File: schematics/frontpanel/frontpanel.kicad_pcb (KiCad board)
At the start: 2 copper layers, 72.4 x 21.6 mm, 10 parts, among them J1 Conn_01x02_Male, J2 Conn_01x02_Male, J3 Conn_01x03_Male, J4 Conn_01x03_Male, SW1 SW_Push, SW2 SW_Push

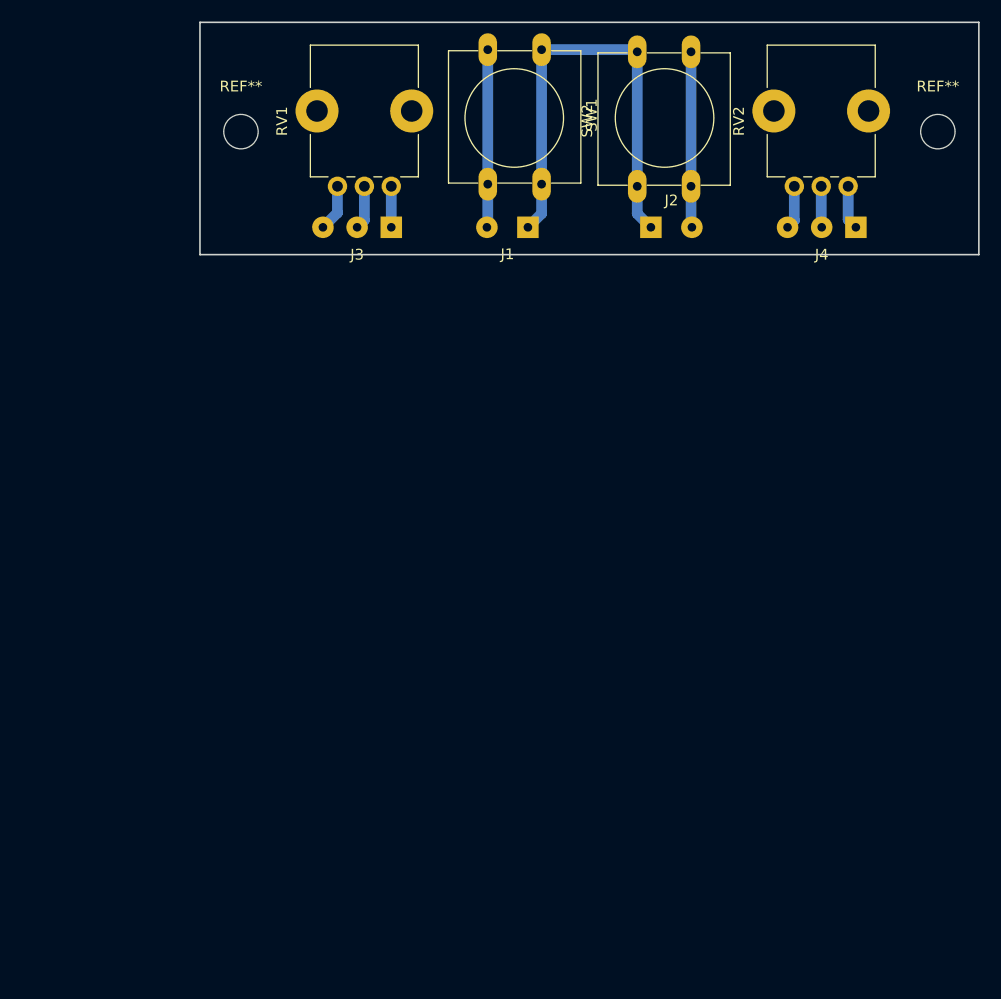
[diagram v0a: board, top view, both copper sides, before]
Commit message: Updated front panel PCB for v1
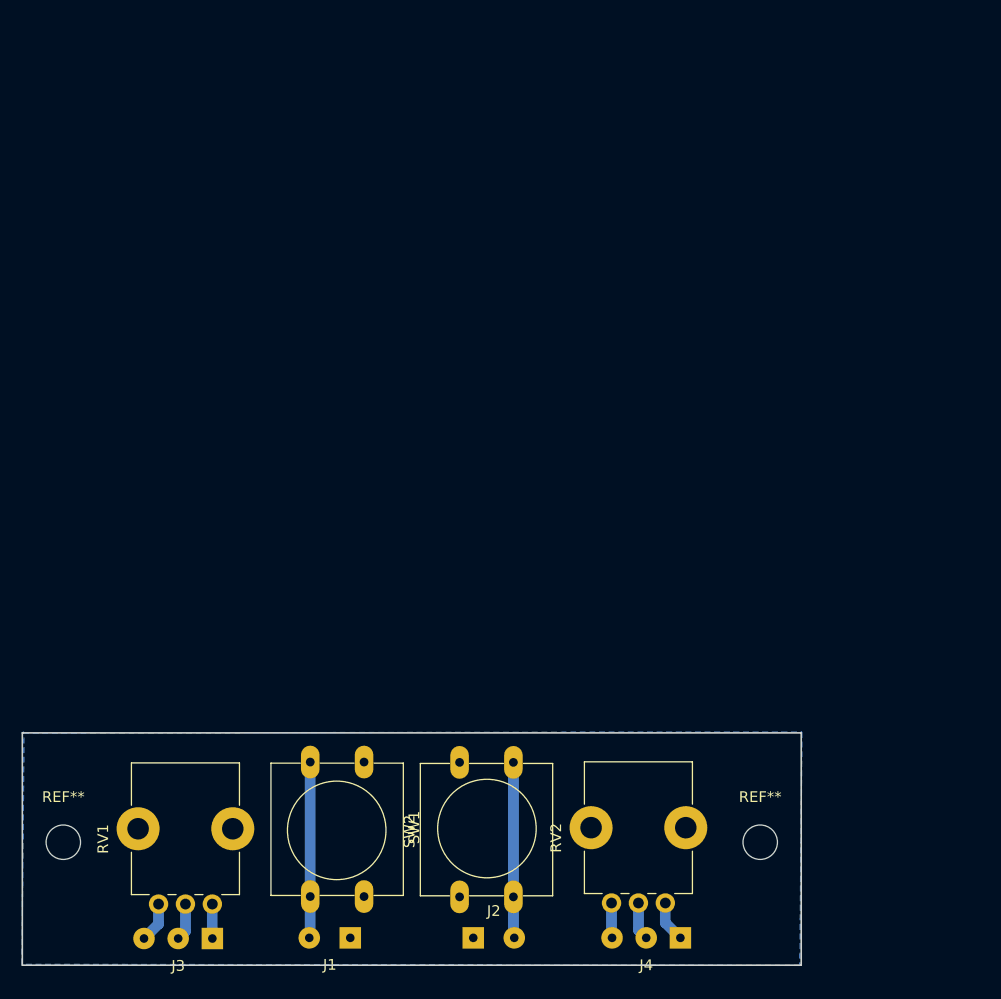
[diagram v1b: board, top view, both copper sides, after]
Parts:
- moved RV1 68.8 mm to (58.3, 126.4)
- moved RV2 68.7 mm to (100.4, 126.3)
- moved SW1 68.2 mm to (72.4, 113.2)
- moved J3 68.2 mm to (58.3, 129.6)
- moved REF** 68.1 mm to (109.2, 120.7)
- moved REF** 68.1 mm to (44.5, 120.7)
- moved SW2 68.1 mm to (81.3, 125.7)
- moved J1 68.1 mm to (71.1, 129.5)
- moved J2 68.1 mm to (82.5, 129.5)
- moved J4 68.0 mm to (101.8, 129.5)
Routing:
- net Net-(J1-Pad1): track 42.8 -> 0.28 mm
- net Net-(J4-Pad3): track 4.07 -> 3.26 mm
- net Net-(J3-Pad3): track 4.37 -> 3.76 mm
- net Net-(J3-Pad2): track 4.09 -> 3.48 mm
- net Net-(J3-Pad1): track 3.81 -> 3.20 mm
- added copper zone on B.Cu, net Net-(J1-Pad1)
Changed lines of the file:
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@@
     (thickness 1.6)
     (drawings 6)
-    (tracks 24)
+    (tracks 18)
     (zones 0)
     (modules 10)
@@
   )
   (module Potentiometer_THT:Potentiometer_Alps_RK09K_Single_Vertical (layer F.Cu)
-    (at 117.39 59.69 90)
+    (at 100.4 126.3 90)
     (descr "Potentiometer, vertical, Alps RK09K Single, http://www.alps.com/prod/info/E/HTML/Potentiometer/RotaryPotentiometers/RK09K/RK09K_list.html")
     (tags "Potentiometer vertical Alps RK09K Single")
@@
   )
   (module Connector_Wire:SolderWirePad_1x02_P3.81mm_Drill0.8mm (layer F.Cu)
-    (at 87.63 63.5 180)
+    (at 71.12 129.54 180)
     (descr "Wire solder connection")
     (tags connector)
@@
   )
   (module Connector_Wire:SolderWirePad_1x02_P3.81mm_Drill0.8mm (layer F.Cu)
-    (at 99.06 63.5)
+    (at 82.55 129.54)
     (descr "Wire solder connection")
     (tags connector)
@@
   )
   (module Connector_Wire:SolderWirePad_1x03_P3.175mm_Drill0.8mm (layer F.Cu)
-    (at 74.93 63.5 180)
+    (at 58.3 129.6 180)
     (descr "Wire solder connection")
     (tags connector)
@@
   )
   (module Connector_Wire:SolderWirePad_1x03_P3.175mm_Drill0.8mm (layer F.Cu)
-    (at 118.11 63.5 180)
+    (at 101.8 129.54 180)
     (descr "Wire solder connection")
     (tags connector)
@@
   )
   (module Potentiometer_THT:Potentiometer_Alps_RK09K_Single_Vertical (layer F.Cu)
-    (at 74.93 59.69 90)
+    (at 58.3 126.4 90)
     (descr "Potentiometer, vertical, Alps RK09K Single, http://www.alps.com/prod/info/E/HTML/Potentiometer/RotaryPotentiometers/RK09K/RK09K_list.html")
     (tags "Potentiometer vertical Alps RK09K Single")
@@
   )
   (module Button_Switch_THT:SW_PUSH-12mm (layer F.Cu)
-    (at 88.9 46.99 270)
+    (at 72.4 113.2 270)
     (descr "SW PUSH 12mm https://www.e-switch.com/system/asset/product_line/data_sheet/143/TL1100.pdf")
     (tags "tact sw push 12mm")
@@
   )
   (module Button_Switch_THT:SW_PUSH-12mm (layer F.Cu)
-    (at 97.79 59.69 90)
+    (at 81.28 125.73 90)
     (descr "SW PUSH 12mm https://www.e-switch.com/system/asset/product_line/data_sheet/143/TL1100.pdf")
     (tags "tact sw push 12mm")
@@
   )
   (module MountingHole:MountingHole_3.2mm_M3 (layer F.Cu)
-    (at 125.73 54.61)
+    (at 109.22 120.65)
     (descr "Mounting Hole 3.2mm, no annular, M3")
     (tags "mounting hole 3.2mm no annular m3")
@@
   )
   (module MountingHole:MountingHole_3.2mm_M3 (layer F.Cu)
-    (at 60.96 54.61)
+    (at 44.45 120.65)
     (descr "Mounting Hole 3.2mm, no annular, M3")
     (tags "mounting hole 3.2mm no annular m3")
@@
   )
   (dimension 21.59 (width 0.3) (layer Dwgs.User)
-    (gr_text "21,590 mm" (at 49.97 55.245 90) (layer Dwgs.User)
+    (gr_text "21,590 mm" (at 33.46 121.285 90) (layer Dwgs.User)
       (effects (font (size 1.5 1.5) (thickness 0.3)))
     )
-    (feature1 (pts (xy 57.15 44.45) (xy 51.483579 44.45)))
-    (feature2 (pts (xy 57.15 66.04) (xy 51.483579 66.04)))
-    (crossbar (pts (xy 52.07 66.04) (xy 52.07 44.45)))
-    (arrow1a (pts (xy 52.07 44.45) (xy 52.656421 45.576504)))
-    (arrow1b (pts (xy 52.07 44.45) (xy 51.483579 45.576504)))
-    (arrow2a (pts (xy 52.07 66.04) (xy 52.656421 64.913496)))
-    (arrow2b (pts (xy 52.07 66.04) (xy 51.483579 64.913496)))
+    (feature1 (pts (xy 40.64 110.49) (xy 34.973579 110.49)))
+    (feature2 (pts (xy 40.64 132.08) (xy 34.973579 132.08)))
+    (crossbar (pts (xy 35.56 132.08) (xy 35.56 110.49)))
+    (arrow1a (pts (xy 35.56 110.49) (xy 36.146421 111.616504)))
+    (arrow1b (pts (xy 35.56 110.49) (xy 34.973579 111.616504)))
+    (arrow2a (pts (xy 35.56 132.08) (xy 36.146421 130.953496)))
+    (arrow2b (pts (xy 35.56 132.08) (xy 34.973579 130.953496)))
   )
   (dimension 72.39 (width 0.3) (layer Dwgs.User)
-    (gr_text "72,390 mm" (at 93.345 73.22) (layer Dwgs.User)
+    (gr_text "72,390 mm" (at 76.835 139.26) (layer Dwgs.User)
       (effects (font (size 1.5 1.5) (thickness 0.3)))
     )
-    (feature1 (pts (xy 129.54 66.04) (xy 129.54 71.706421)))
-    (feature2 (pts (xy 57.15 66.04) (xy 57.15 71.706421)))
-    (crossbar (pts (xy 57.15 71.12) (xy 129.54 71.12)))
-    (arrow1a (pts (xy 129.54 71.12) (xy 128.413496 71.706421)))
-    (arrow1b (pts (xy 129.54 71.12) (xy 128.413496 70.533579)))
-    (arrow2a (pts (xy 57.15 71.12) (xy 58.276504 71.706421)))
-    (arrow2b (pts (xy 57.15 71.12) (xy 58.276504 70.533579)))
-  )
-  (gr_line (start 57.15 66.04) (end 57.15 44.45) (layer Edge.Cuts) (width 0.15))
-  (gr_line (start 129.54 66.04) (end 57.15 66.04) (layer Edge.Cuts) (width 0.15))
-  (gr_line (start 129.54 44.45) (end 129.54 66.04) (layer Edge.Cuts) (width 0.15))
-  (gr_line (start 57.15 44.45) (end 129.54 44.45) (layer Edge.Cuts) (width 0.15))
-  (segment (start 97.79 62.23) (end 99.06 63.5) (width 1) (layer B.Cu) (net 1))
-  (segment (start 97.79 59.69) (end 97.79 62.23) (width 1) (layer B.Cu) (net 1))
-  (segment (start 88.9 62.23) (end 87.63 63.5) (width 1) (layer B.Cu) (net 1))
-  (segment (start 88.9 59.49) (end 88.9 62.23) (width 1) (layer B.Cu) (net 1))
-  (segment (start 88.9 46.99) (end 88.9 59.49) (width 1) (layer B.Cu) (net 1))
-  (segment (start 97.79 47.19) (end 97.79 59.69) (width 1) (layer B.Cu) (net 1))
-  (segment (start 97.59 46.99) (end 97.79 47.19) (width 1) (layer B.Cu) (net 1))
-  (segment (start 88.9 46.99) (end 97.59 46.99) (width 1) (layer B.Cu) (net 1))
-  (segment (start 83.9 63.42) (end 83.82 63.5) (width 1) (layer B.Cu) (net 2))
-  (segment (start 83.9 46.99) (end 83.9 63.42) (width 1) (layer B.Cu) (net 2))
-  (segment (start 102.79 46.5296) (end 102.79 47.19) (width 1) (layer B.Cu) (net 9))
-  (segment (start 74.93 59.69) (end 74.93 63.5) (width 1) (layer B.Cu) (net 3))
-  (segment (start 72.43 62.825) (end 71.755 63.5) (width 1) (layer B.Cu) (net 4))
-  (segment (start 72.43 59.69) (end 72.43 62.825) (width 1) (layer B.Cu) (net 4))
-  (segment (start 69.93 62.15) (end 68.58 63.5) (width 1) (layer B.Cu) (net 5))
-  (segment (start 69.93 59.69) (end 69.93 62.15) (width 1) (layer B.Cu) (net 5))
-  (segment (start 112.39 62.87) (end 111.76 63.5) (width 1) (layer B.Cu) (net 6))
-  (segment (start 112.39 59.69) (end 112.39 62.87) (width 1) (layer B.Cu) (net 6))
-  (segment (start 114.89 63.455) (end 114.935 63.5) (width 1) (layer B.Cu) (net 7))
-  (segment (start 114.89 59.69) (end 114.89 63.455) (width 1) (layer B.Cu) (net 7))
-  (segment (start 117.39 62.78) (end 118.11 63.5) (width 1) (layer B.Cu) (net 8))
-  (segment (start 117.39 59.69) (end 117.39 62.78) (width 1) (layer B.Cu) (net 8))
-  (segment (start 102.79 63.42) (end 102.87 63.5) (width 1) (layer B.Cu) (net 9))
-  (segment (start 102.79 47.19) (end 102.79 63.42) (width 1) (layer B.Cu) (net 9))
+    (feature1 (pts (xy 113.03 132.08) (xy 113.03 137.746421)))
+    (feature2 (pts (xy 40.64 132.08) (xy 40.64 137.746421)))
+    (crossbar (pts (xy 40.64 137.16) (xy 113.03 137.16)))
+    (arrow1a (pts (xy 113.03 137.16) (xy 111.903496 137.746421)))
+    (arrow1b (pts (xy 113.03 137.16) (xy 111.903496 136.573579)))
+    (arrow2a (pts (xy 40.64 137.16) (xy 41.766504 137.746421)))
+    (arrow2b (pts (xy 40.64 137.16) (xy 41.766504 136.573579)))
+  )
+  (gr_line (start 40.64 132.08) (end 40.64 110.49) (layer Edge.Cuts) (width 0.15))
+  (gr_line (start 113.03 132.08) (end 40.64 132.08) (layer Edge.Cuts) (width 0.15))
+  (gr_line (start 113.03 110.49) (end 113.03 132.08) (layer Edge.Cuts) (width 0.15))
+  (gr_line (start 40.64 110.49) (end 113.03 110.49) (layer Edge.Cuts) (width 0.15))
+  (segment (start 81.08 113.03) (end 81.28 113.23) (width 1) (layer B.Cu) (net 1))
+  (segment (start 67.39 129.46) (end 67.31 129.54) (width 1) (layer B.Cu) (net 2))
+  (segment (start 67.39 113.03) (end 67.39 129.46) (width 1) (layer B.Cu) (net 2))
+  (segment (start 58.3 126.4) (end 58.3 129.6) (width 1) (layer B.Cu) (net 3))
+  (segment (start 55.8 128.925) (end 55.125 129.6) (width 1) (layer B.Cu) (net 4))
+  (segment (start 55.8 126.4) (end 55.8 128.925) (width 1) (layer B.Cu) (net 4))
+  (segment (start 53.3 128.25) (end 51.95 129.6) (width 1) (layer B.Cu) (net 5))
+  (segment (start 53.3 126.4) (end 53.3 128.25) (width 1) (layer B.Cu) (net 5))
+  (segment (start 95.4 129.49) (end 95.45 129.54) (width 1) (layer B.Cu) (net 6))
+  (segment (start 95.4 126.3) (end 95.4 129.49) (width 1) (layer B.Cu) (net 6))
+  (segment (start 98.38 129.495) (end 98.425 129.54) (width 1) (layer B.Cu) (net 7))
+  (segment (start 97.9 128.815) (end 98.625 129.54) (width 1) (layer B.Cu) (net 7))
+  (segment (start 97.9 126.3) (end 97.9 128.815) (width 1) (layer B.Cu) (net 7))
+  (segment (start 100.4 128.14) (end 101.8 129.54) (width 1) (layer B.Cu) (net 8))
+  (segment (start 100.4 126.3) (end 100.4 128.14) (width 1) (layer B.Cu) (net 8))
+  (segment (start 86.28 112.5696) (end 86.28 113.23) (width 1) (layer B.Cu) (net 9))
+  (segment (start 86.28 129.46) (end 86.36 129.54) (width 1) (layer B.Cu) (net 9))
+  (segment (start 86.28 113.23) (end 86.28 129.46) (width 1) (layer B.Cu) (net 9))
+  (zone (net 1) (net_name "Net-(J1-Pad1)") (layer B.Cu) (hatch edge 0.508)
+    (connect_pads (clearance 0.508))
+    (min_thickness 0.254)
+    (fill yes (arc_segments 16) (thermal_gap 0.508) (thermal_bridge_width 0.508))
+    (polygon
+      (pts
+        (xy 40.7 110.5) (xy 113.1 110.4) (xy 112.9 132.1) (xy 40.6 132) (xy 40.8 110.4)
+        (xy 40.6 110.5) (xy 40.8 110.5)
+      )
+    )
+  )
 )

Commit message: PCBs updated
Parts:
- removed the REF** at (109.2, 120.7)
- removed the REF** at (44.5, 120.7)
- added REF**: MountingHole_3.2mm_M3, MountingHole:MountingHole_3.2mm_M3, F.Cu at (109.0, 119.5)
- added REF**: MountingHole_3.2mm_M3, MountingHole:MountingHole_3.2mm_M3, F.Cu at (44.8, 119.4)
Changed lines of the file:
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@@
     (thickness 1.6)
     (drawings 6)
-    (tracks 18)
+    (tracks 19)
     (zones 0)
     (modules 10)
@@
     (last_trace_width 1)
     (trace_clearance 0.5)
-    (zone_clearance 0.508)
+    (zone_clearance 0.6)
     (zone_45_only no)
     (trace_min 0.2)
@@
     (visible_elements FFFFFF7F)
     (pcbplotparams
-      (layerselection 0x010fc_ffffffff)
+      (layerselection 0x00000_fffffffe)
       (usegerberextensions false)
       (usegerberattributes false)
       (usegerberadvancedattributes false)
       (creategerberjobfile false)
-      (excludeedgelayer true)
+      (excludeedgelayer false)
       (linewidth 0.100000)
       (plotframeref false)
@@
       (hpglpenspeed 20)
       (hpglpendiameter 15.000000)
-      (psnegative false)
+      (psnegative true)
       (psa4output false)
-      (plotreference true)
-      (plotvalue true)
+      (plotreference false)
+      (plotvalue false)
       (plotinvisibletext false)
-      (padsonsilk false)
+      (padsonsilk true)
       (subtractmaskfromsilk false)
-      (outputformat 1)
+      (outputformat 4)
       (mirror false)
-      (drillshape 1)
+      (drillshape 2)
       (scaleselection 1)
       (outputdirectory ""))
@@
   )
   (module MountingHole:MountingHole_3.2mm_M3 (layer F.Cu)
-    (at 109.22 120.65)
+    (at 109 119.5)
     (descr "Mounting Hole 3.2mm, no annular, M3")
     (tags "mounting hole 3.2mm no annular m3")
@@
   )
   (module MountingHole:MountingHole_3.2mm_M3 (layer F.Cu)
-    (at 44.45 120.65)
+    (at 44.8 119.4)
     (descr "Mounting Hole 3.2mm, no annular, M3")
     (tags "mounting hole 3.2mm no annular m3")
@@
     )
     (pad 1 np_thru_hole circle (at 0 0) (size 3.2 3.2) (drill 3.2) (layers *.Cu *.Mask))
+  )
+  (dimension 72.39 (width 0.3) (layer Dwgs.User)
+    (gr_text "72,390 mm" (at 76.835 139.26) (layer Dwgs.User)
+      (effects (font (size 1.5 1.5) (thickness 0.3)))
+    )
+    (feature1 (pts (xy 113.03 132.08) (xy 113.03 137.746421)))
+    (feature2 (pts (xy 40.64 132.08) (xy 40.64 137.746421)))
+    (crossbar (pts (xy 40.64 137.16) (xy 113.03 137.16)))
+    (arrow1a (pts (xy 113.03 137.16) (xy 111.903496 137.746421)))
+    (arrow1b (pts (xy 113.03 137.16) (xy 111.903496 136.573579)))
+    (arrow2a (pts (xy 40.64 137.16) (xy 41.766504 137.746421)))
+    (arrow2b (pts (xy 40.64 137.16) (xy 41.766504 136.573579)))
   )
   (dimension 21.59 (width 0.3) (layer Dwgs.User)
@@
     (arrow2b (pts (xy 35.56 132.08) (xy 34.973579 130.953496)))
   )
-  (dimension 72.39 (width 0.3) (layer Dwgs.User)
-    (gr_text "72,390 mm" (at 76.835 139.26) (layer Dwgs.User)
-      (effects (font (size 1.5 1.5) (thickness 0.3)))
-    )
-    (feature1 (pts (xy 113.03 132.08) (xy 113.03 137.746421)))
-    (feature2 (pts (xy 40.64 132.08) (xy 40.64 137.746421)))
-    (crossbar (pts (xy 40.64 137.16) (xy 113.03 137.16)))
-    (arrow1a (pts (xy 113.03 137.16) (xy 111.903496 137.746421)))
-    (arrow1b (pts (xy 113.03 137.16) (xy 111.903496 136.573579)))
-    (arrow2a (pts (xy 40.64 137.16) (xy 41.766504 137.746421)))
-    (arrow2b (pts (xy 40.64 137.16) (xy 41.766504 136.573579)))
-  )
   (gr_line (start 40.64 132.08) (end 40.64 110.49) (layer Edge.Cuts) (width 0.15))
   (gr_line (start 113.03 132.08) (end 40.64 132.08) (layer Edge.Cuts) (width 0.15))
@@
   (segment (start 81.08 113.03) (end 81.28 113.23) (width 1) (layer B.Cu) (net 1))
   (segment (start 67.39 129.46) (end 67.31 129.54) (width 1) (layer B.Cu) (net 2))
-  (segment (start 67.39 113.03) (end 67.39 129.46) (width 1) (layer B.Cu) (net 2))
+  (segment (start 67.4 129.45) (end 67.31 129.54) (width 1) (layer B.Cu) (net 2))
+  (segment (start 67.4 113.2) (end 67.4 129.45) (width 1) (layer B.Cu) (net 2))
   (segment (start 58.3 126.4) (end 58.3 129.6) (width 1) (layer B.Cu) (net 3))
   (segment (start 55.8 128.925) (end 55.125 129.6) (width 1) (layer B.Cu) (net 4))
@@
   (segment (start 86.28 113.23) (end 86.28 129.46) (width 1) (layer B.Cu) (net 9))
   (zone (net 1) (net_name "Net-(J1-Pad1)") (layer B.Cu) (hatch edge 0.508)
-    (connect_pads (clearance 0.508))
+    (connect_pads (clearance 0.6))
     (min_thickness 0.254)
     (fill yes (arc_segments 16) (thermal_gap 0.508) (thermal_bridge_width 0.508))
     (polygon
       (pts
-        (xy 40.7 110.5) (xy 113.1 110.4) (xy 112.9 132.1) (xy 40.6 132) (xy 40.8 110.4)
-        (xy 40.6 110.5) (xy 40.8 110.5)
+        (xy 40.775 110.5) (xy 113.1 110.5) (xy 113 132) (xy 40.7 132) (xy 40.7 110.4)
       )
     )
